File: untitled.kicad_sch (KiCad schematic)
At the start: 39 parts, among them U17 OPA388, U3 MAX9939, U4 TLV3501AID, U5 DAC60501, U7 ADC10065

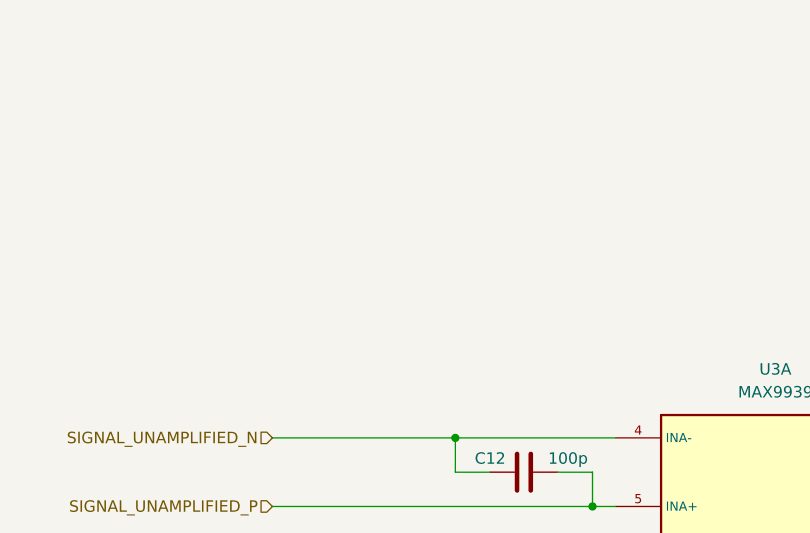
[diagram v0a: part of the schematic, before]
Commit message: V1 completed, starting on V2 after consultation with mr. Chalupa
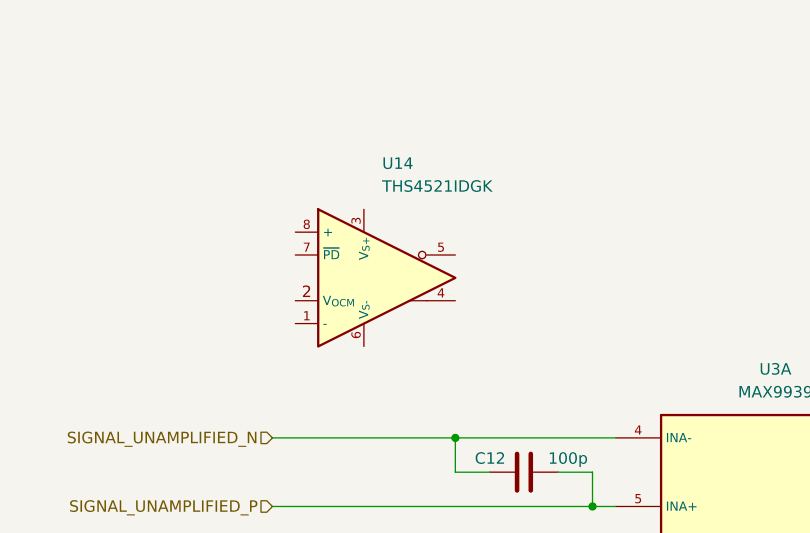
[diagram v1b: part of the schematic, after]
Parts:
- added U14: THS4521IDGK, Package_SO:VSSOP-8_3.0x3.0mm_P0.65mm, symbol Amplifier_Difference:THS4521IDGK
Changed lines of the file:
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@@
+	)
+	(symbol
+		(lib_id "Amplifier_Difference:THS4521IDGK")
+		(at 83.82 46.99 0)
+		(unit 1)
+		(exclude_from_sim no)
+		(in_bom yes)
+		(on_board yes)
+		(dnp no)
+		(fields_autoplaced yes)
+		(property "Reference" "U14"
+			(at 83.2994 34.29 0)
+			(effects
+				(font
+					(size 1.27 1.27)
+				)
+				(justify left)
+			)
+		)
+		(property "Value" "THS4521IDGK"
+			(at 83.2994 36.83 0)
+			(effects
+				(font
+					(size 1.27 1.27)
+				)
+				(justify left)
+			)
+		)
+		(property "Footprint" "Package_SO:VSSOP-8_3.0x3.0mm_P0.65mm"
+			(at 83.82 66.04 0)
+			(effects
+				(font
+					(size 1.27 1.27)
+				)
+				(hide yes)
+			)
+		)
+		(property "Datasheet" "https://www.ti.com/lit/ds/symlink/ths4521.pdf"
+			(at 83.82 63.5 0)
+			(effects
+				(font
+					(size 1.27 1.27)
+				)
+				(hide yes)
+			)
+		)
+		(property "Description" "Very Low Power, Negative Rail Input, Rail to Rail Output, Fully Differential Amplifier, VSSOP-8"
+			(at 83.82 46.99 0)
+			(effects
+				(font
+					(size 1.27 1.27)
+				)
+				(hide yes)
+			)
+		)
+		(pin "6"
+		)
+		(pin "7"
+		)
+		(pin "4"
+		)
+		(pin "1"
+		)
+		(pin "3"
+		)
+		(pin "2"
+		)
+		(pin "8"
+		)
+		(pin "5"
+		)
+		(instances
+			(project "ultrasonic_V3_HW"
+				(path "/731d4032-cf8d-4f76-95ca-2ec44c8e0816/bbbd27e3-755b-468e-8e26-bb40916e3b9a"
+					(reference "U14")
+					(unit 1)
+				)
+			)
+		)
 	)
 	(symbol

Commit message: V2 finished
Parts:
- removed C10, C11: 1u, Capacitor_SMD:C_0603_1608Metric_Pad1.08x0.95mm_HandSolder, symbol Device:C
- removed C9: 100n, Capacitor_SMD:C_0603_1608Metric_Pad1.08x0.95mm_HandSolder, symbol Device:C
- removed R17: 1k, Resistor_SMD:R_0603_1608Metric_Pad0.98x0.95mm_HandSolder, symbol Device:R
- removed U17: OPA388, Package_SO:VSSOP-8_3.0x3.0mm_P0.65mm, symbol 10_ICs:OPA388
- added C100, C97, C98, C99: 200p, Capacitor_SMD:C_0603_1608Metric_Pad1.08x0.95mm_HandSolder, symbol Device:C
- added C101: 1n, Capacitor_SMD:C_0603_1608Metric_Pad1.08x0.95mm_HandSolder, symbol Device:C
- added C102, C104: 2u2, Capacitor_SMD:C_0805_2012Metric_Pad1.18x1.45mm_HandSolder, symbol Device:C
- added C103, C105, C110: 100n, Capacitor_SMD:C_0603_1608Metric_Pad1.08x0.95mm_HandSolder, symbol Device:C
- added C106, C107: C, Capacitor_SMD:C_0603_1608Metric_Pad1.08x0.95mm_HandSolder, symbol Device:C
- added R86: 200k, Resistor_SMD:R_0603_1608Metric_Pad0.98x0.95mm_HandSolder, symbol Device:R
- added R87: R, Resistor_SMD:R_0603_1608Metric_Pad0.98x0.95mm_HandSolder, symbol Device:R
- added U17: NE5532, Package_SO:SOIC-8_3.9x4.9mm_P1.27mm, symbol Amplifier_Operational:NE5532
- added U25: ADP7142ARDZ-3.3, Package_SO:SOIC-8-1EP_3.9x4.9mm_P1.27mm_EP2.29x3mm, symbol Regulator_Linear:ADP7142ARDZ-3.3
- C1: value 100p -> 120p
- C12: value 100p -> 100n
- C24: value C -> 100p
- C8: value C -> 120p
- R14: value R -> 20; now in the parts list
- R16: value 1k -> 10; now fitted
- R18: value 0 -> 200k
- R19: value 1k -> 200k; now fitted
- R21: value 1k -> 10k; now fitted
- R23: value R -> 10k
- R7: value 10 -> 20
- R72: value 0 -> 200k; now fitted
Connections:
- net AMPLIFIED_SIGNAL_N: now also R29.2, U4.3 (+), C106.1; no longer R8.2, U3.6 (OUTB)
- net AMPLIFIED_SIGNAL_P: now also C1.2, R7.1, C107.1; no longer C24.2, R18.2, R23.1, R5.1, U3.8 (OUTA)
- net DAC_COMPARATOR_REF: now also R16.2; no longer U4.2 (-)
- net GND: now also C12.1, R23.2, U14.6 (V_{S-}), C101.1, C102.1, C103.2, C104.1, C105.2, C110.2, U17.4 (V-), U25.4 (GND), U25.9 (GND); no longer R21.2
- net P3V3: no longer C14.1, C18.2, C19.2, C7.2, C78.1, R15.2, R22.2, U3.9 (VCC), U4.7 (V+), U5.1 (VDD), U7.10 (VDDA), U7.2 (VDDA), U7.9 (VDDA)
- net SIGNAL_UNAMPLIFIED_N: now also R18.2, U14.8 (+), C97.2; no longer C12.2, U3.4 (INA-)
- net SIGNAL_UNAMPLIFIED_P: now also R19.2, U14.1 (-), C98.2; no longer C12.1, U3.5 (INA+)
- net P3V3_A: now reaches R21.1
- net P3V3_A: now also C13.2, C14.1, C18.2, C19.2, C7.2, C78.1, R15.2, R22.2, U14.3 (V_{S+}), U3.9 (VCC), U4.7 (V+), U5.1 (VDD), U5.10 (VREFIO), U7.10 (VDDA), U7.2 (VDDA), U7.9 (VDDA), C102.2, C103.1, C110.1, U25.1 (VOUT), U25.2 (VOUT), U25.3 (SENSE/ADJ); no longer R19.2
- net at R16.1: now also C24.2, U4.2 (-); no longer R72.2
- net Vcom: now reaches C23.2, U7.4 (VCOM)
- net Vcom: now also R25.2, R87.2; no longer R25.1
- net at U7.13 (VIN+): now also R25.1, C106.2; no longer R23.2
- net HALF_VDDA: now reaches U14.2 (V_{OCM})
- net HALF_VDDA: now also R72.2, R86.1, U17.1, U17.2 (-)
- net at U14.4: now also R19.1, R72.1, C98.1, C99.2
- net at U14.5: now also R18.1, C100.2, C97.1, R86.2
- net CHARGE_AMP_SHT: now reaches U14.7 (~{PD})
- removed net AMPLIFIED_SIGNAL: R18.1, R7.2, R72.1
- removed net P3V_REF: C13.2, R19.1, U5.10 (VREFIO)
- new net: R5.1, R7.2, U3.8 (OUTA)
- new net: R14.2, R8.2, U3.6 (OUTB)
- new net: R21.2, R23.1, U17.3 (+)
- new net: C100.1, U3.4 (INA-)
- new net: C99.1, U3.5 (INA+)
- new net: C107.2, R87.1, U7.12 (VIN-)
- new net: C101.2, U25.6 (SS)
- new net P12V: C104.2, C105.1, C12.2, U17.8 (V+), U25.7 (VIN), U25.8 (VIN)
- new net P3V3_A_EN: U25.5 (EN)
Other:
- note added: "Add fully diferential amplifier on the input DONE change the mosfet switch to IC DONE Add charge preamplifier DONE Find better alternative to NE5532"
- note added: "CHARGE AMPLIFIER OPTIONS THS4121/THS4561/THS4521"
- note added: "HALF VDDA REF"
- note added: "IRS pin to fpga?"
- note removed: "Add fully diferential amplifier on the input DONE change the mosfet switch to IC DONE"
- moved on the sheet: C1, C13, C14, C7, C78, R22, R29, R5, R7, R8, U14, U3A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
